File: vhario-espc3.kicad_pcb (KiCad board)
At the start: 2 copper layers, 74 x 34 mm, 56 parts, among them J1 USB_C, J2 Battery, Q1 AO3401A, Q2 2N7002, SW1 RST, SW2 DBG, SW3 PWR, SW4 PCCA, U1 cjmcu117, U2 MCP73831-2-OT, U3 espc3fn4, U4 74HC240PWR, U5 TLV75533PDBV

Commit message: update footprints
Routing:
- net GND: vias 66 -> 82

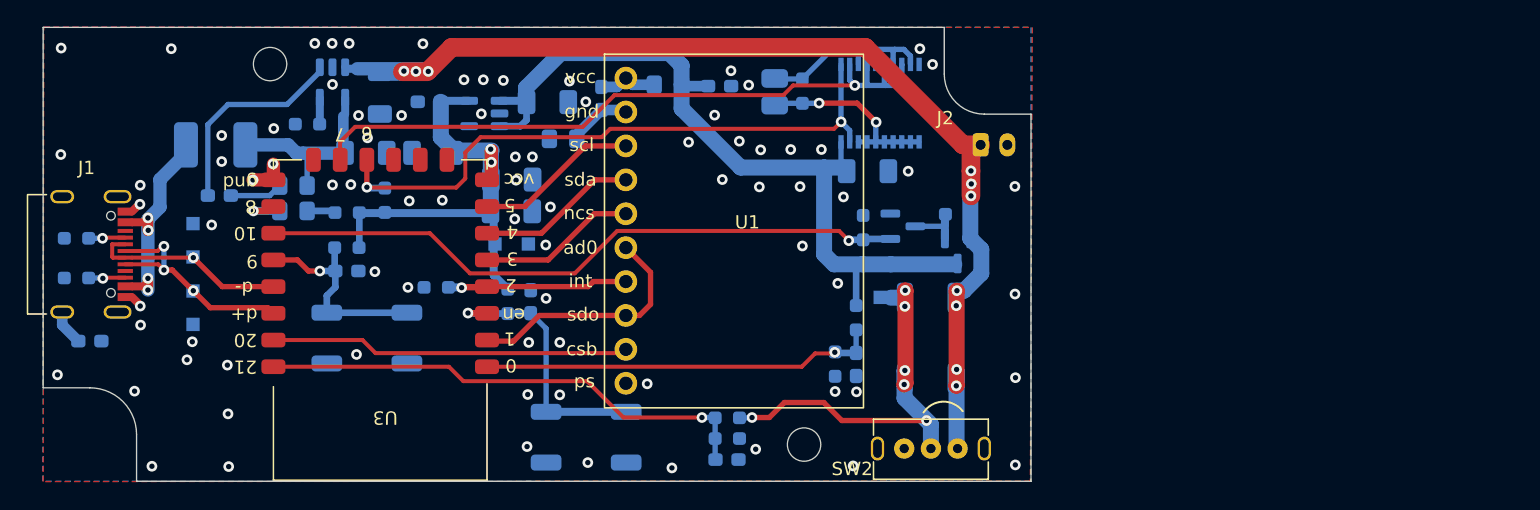
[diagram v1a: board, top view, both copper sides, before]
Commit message: change flash/dbg jumper options
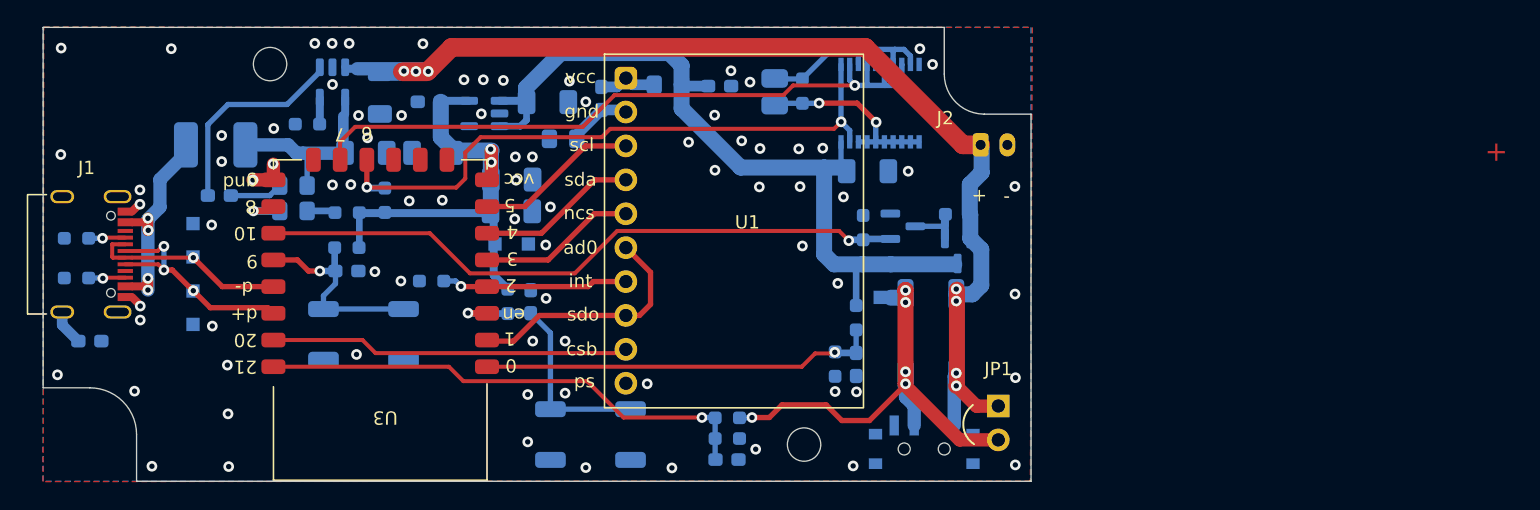
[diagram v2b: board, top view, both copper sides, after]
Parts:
- added JP1: DBG, 0-vhario-espc3:PinSocket_1x02_P2.54mm_Vertical, F.Cu at (160.6, 94.4)
- SW2: footprint 0-vhario-espc3:sk12d07vg3 -> 0-vhario-espc3:SW_SPDT_PCM12; moved to B.Cu
- moved SW2 1.53 mm to (155.0, 97.2), turned to 180 degrees
- moved R1 0.59 mm to (118.1, 85.0)
- moved SW1 0.38 mm to (130.0, 96.5)
- moved SW4 0.37 mm to (113.0, 89.0)
- moved SW3 0.28 mm to (155.5, 89.0)
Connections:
- SW2 pad 1: unconnected-(SW2-Pad1) -> +BATT
- SW2 pad 3: +BATT -> unconnected-(SW2-Pad3)
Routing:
- net Net-(D5-Pad2): track 30.0 -> 34.6 mm, vias 6 -> 5
- net /DRDY: track 15.4 -> 14.0 mm
- net +BATT: track 80.1 -> 81.2 mm, vias 10 -> 7
- net GND: vias 82 -> 81
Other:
- board text added: "+"
- board text added: "-"
